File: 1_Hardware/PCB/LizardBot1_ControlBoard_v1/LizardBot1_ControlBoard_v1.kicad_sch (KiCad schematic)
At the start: 0 parts

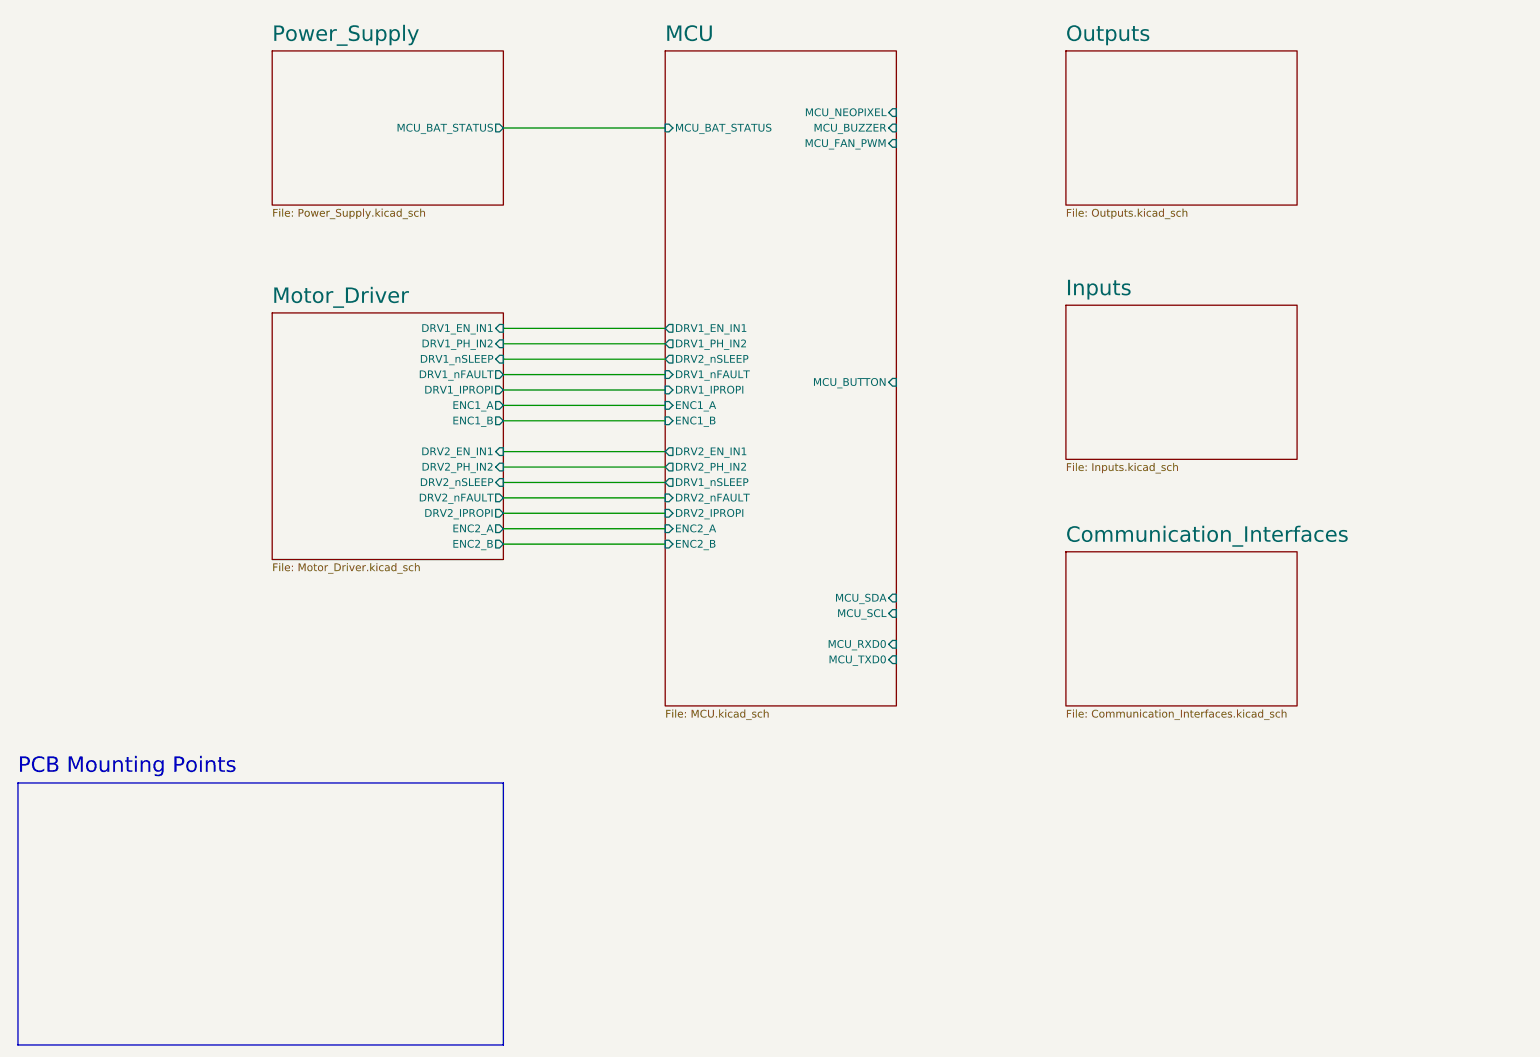
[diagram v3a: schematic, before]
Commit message: Added Peripherals schematic
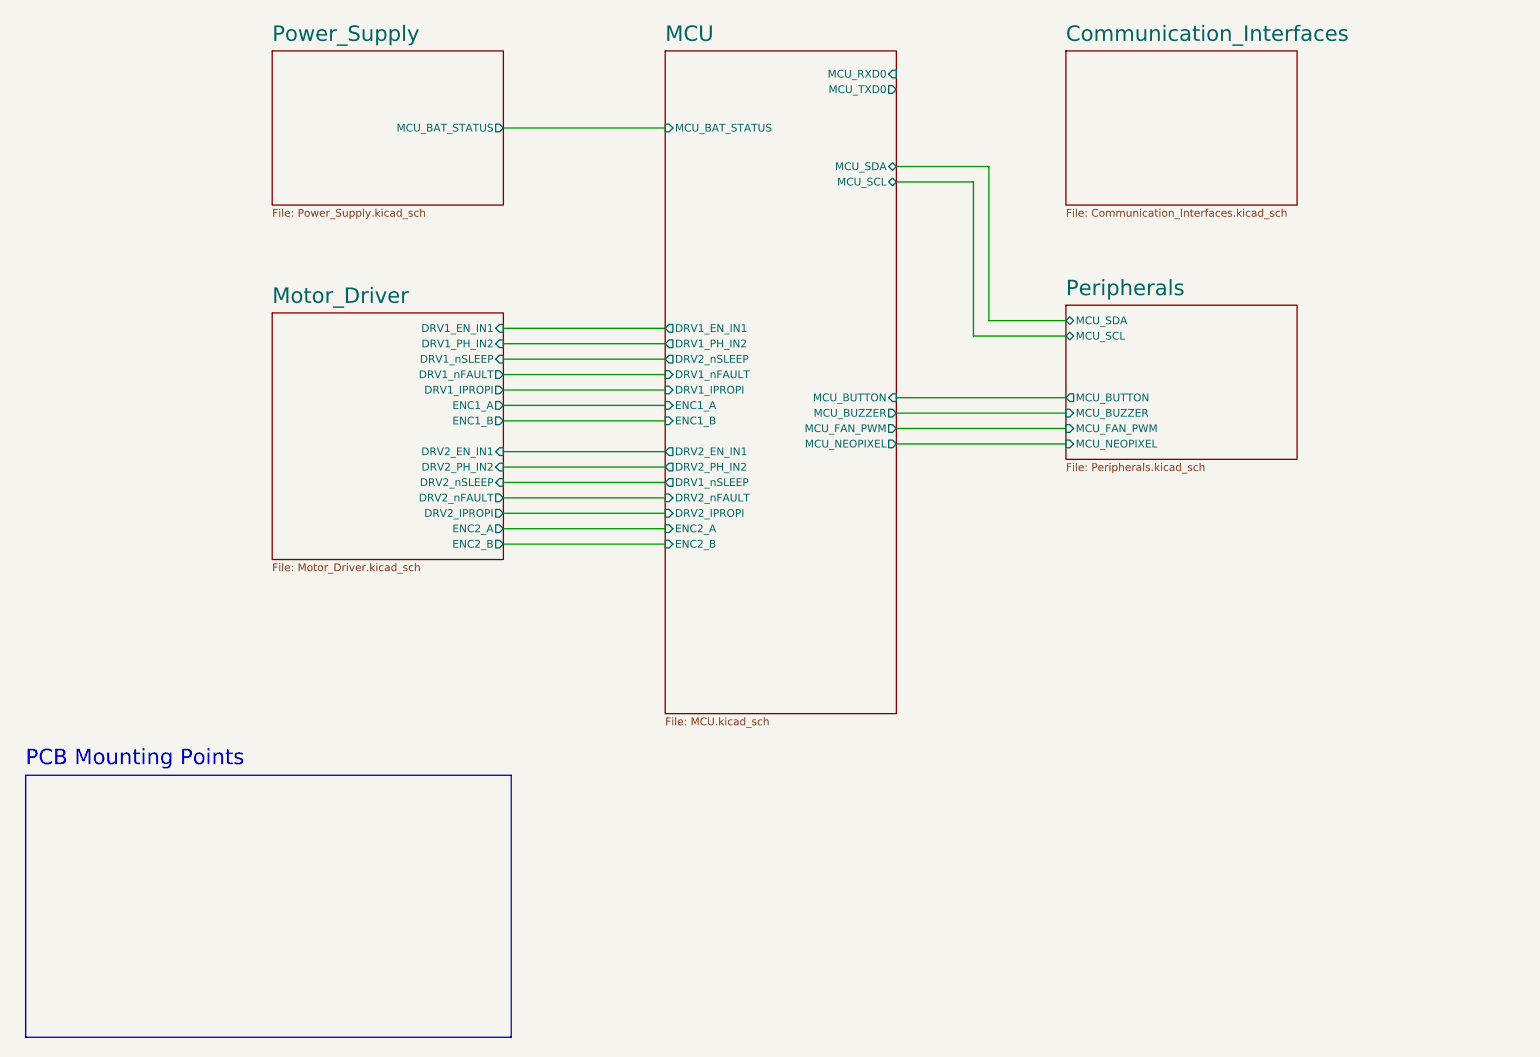
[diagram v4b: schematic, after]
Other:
- sheet Outputs renamed Peripherals
- removed sheet Inputs
- sheet Peripherals: file Outputs.kicad_sch -> Peripherals.kicad_sch
- sheet Peripherals ports: added MCU_BUTTON, MCU_BUZZER, MCU_FAN_PWM, MCU_NEOPIXEL, MCU_SCL, MCU_SDA; removed none
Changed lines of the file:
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@@
+	(wire
+		(pts
+			(xy 163.83 87.63) (xy 191.77 87.63)
+		)
+		(stroke
+			(width 0)
+			(type default)
+		)
+	)
 	(wire
 		(pts
@@
 	(wire
 		(pts
+			(xy 179.07 46.99) (xy 163.83 46.99)
+		)
+		(stroke
+			(width 0)
+			(type default)
+		)
+	)
+	(wire
+		(pts
 			(xy 99.06 93.98) (xy 125.73 93.98)
 		)
@@
 	(wire
 		(pts
+			(xy 163.83 85.09) (xy 191.77 85.09)
+		)
+		(stroke
+			(width 0)
+			(type default)
+		)
+	)
+	(wire
+		(pts
 			(xy 99.06 81.28) (xy 125.73 81.28)
 		)
@@
 	(wire
 		(pts
+			(xy 163.83 92.71) (xy 191.77 92.71)
+		)
+		(stroke
+			(width 0)
+			(type default)
+		)
+	)
+	(wire
+		(pts
 			(xy 99.06 40.64) (xy 125.73 40.64)
 		)
@@
 	(wire
 		(pts
+			(xy 176.53 74.93) (xy 191.77 74.93)
+		)
+		(stroke
+			(width 0)
+			(type default)
+		)
+	)
+	(wire
+		(pts
+			(xy 176.53 74.93) (xy 176.53 49.53)
+		)
+		(stroke
+			(width 0)
+			(type default)
+		)
+	)
+	(wire
+		(pts
+			(xy 163.83 90.17) (xy 191.77 90.17)
+		)
+		(stroke
+			(width 0)
+			(type default)
+		)
+	)
+	(wire
+		(pts
+			(xy 179.07 72.39) (xy 179.07 46.99)
+		)
+		(stroke
+			(width 0)
+			(type default)
+		)
+	)
+	(wire
+		(pts
+			(xy 179.07 72.39) (xy 191.77 72.39)
+		)
+		(stroke
+			(width 0)
+			(type default)
+		)
+	)
+	(wire
+		(pts
+			(xy 176.53 49.53) (xy 163.83 49.53)
+		)
+		(stroke
+			(width 0)
+			(type default)
+		)
+	)
+	(wire
+		(pts
 			(xy 99.06 106.68) (xy 125.73 106.68)
 		)
@@
 	)
 	(rectangle
-		(start 19.05 148.59)
-		(end 99.06 191.77)
+		(start 20.32 147.32)
+		(end 100.33 190.5)
 		(stroke
 			(width 0)
@@
 	(text "PCB Mounting Points"
 		(exclude_from_sim no)
-		(at 19.05 147.32 0)
+		(at 20.32 146.05 0)
 		(effects
 			(font
@@
 	)
 	(sheet
-		(at 191.77 69.85)
-		(size 38.1 25.4)
+		(at 125.73 27.94)
+		(size 38.1 109.22)
 		(fields_autoplaced yes)
 		(stroke
@@
 			(color 0 0 0 0.0000)
 		)
-		(property "Sheetname" "Inputs"
-			(at 191.77 68.5034 0)
-			(effects
-				(font
-					(size 2.54 2.54)
-				)
-				(justify left bottom)
-			)
-		)
-		(property "Sheetfile" "Inputs.kicad_sch"
-			(at 191.77 95.8346 0)
-			(effects
-				(font
-					(size 1.27 1.27)
-				)
-				(justify left top)
-			)
-		)
-		(instances
-			(project "LizardBot1_ControlBoard_v1"
-				(path "/1a674a4d-d877-4d7a-ad57-e0a054705c31"
-					(page "5")
-				)
-			)
-		)
-	)
-	(sheet
-		(at 125.73 27.94)
-		(size 38.1 107.95)
-		(fields_autoplaced yes)
-		(stroke
-			(width 0.1524)
-			(type solid)
-		)
-		(fill
-			(color 0 0 0 0.0000)
-		)
 		(property "Sheetname" "MCU"
 			(at 125.73 26.5934 0)
@@
 		)
 		(property "Sheetfile" "MCU.kicad_sch"
-			(at 125.73 136.4746 0)
+			(at 125.73 137.7446 0)
 			(effects
 				(font
@@
 			)
 		)
+		(pin "MCU_BUZZER" output
+			(at 163.83 87.63 0)
+			(effects
+				(font
+					(size 1.27 1.27)
+				)
+				(justify right)
+			)
+		)
+		(pin "MCU_FAN_PWM" output
+			(at 163.83 90.17 0)
+			(effects
+				(font
+					(size 1.27 1.27)
+				)
+				(justify right)
+			)
+		)
+		(pin "MCU_NEOPIXEL" output
+			(at 163.83 92.71 0)
+			(effects
+				(font
+					(size 1.27 1.27)
+				)
+				(justify right)
+			)
+		)
+		(pin "MCU_BUTTON" input
+			(at 163.83 85.09 0)
+			(effects
+				(font
+					(size 1.27 1.27)
+				)
+				(justify right)
+			)
+		)
+		(pin "MCU_SDA" bidirectional
+			(at 163.83 46.99 0)
+			(effects
+				(font
+					(size 1.27 1.27)
+				)
+				(justify right)
+			)
+		)
+		(pin "MCU_SCL" bidirectional
+			(at 163.83 49.53 0)
+			(effects
+				(font
+					(size 1.27 1.27)
+				)
+				(justify right)
+			)
+		)
 		(pin "MCU_RXD0" input
-			(at 163.83 125.73 0)
-			(effects
-				(font
-					(size 1.27 1.27)
-				)
-				(justify right)
-			)
-		)
-		(pin "MCU_TXD0" input
-			(at 163.83 128.27 0)
-			(effects
-				(font
-					(size 1.27 1.27)
-				)
-				(justify right)
-			)
-		)
-		(pin "MCU_NEOPIXEL" input
-			(at 163.83 38.1 0)
-			(effects
-				(font
-					(size 1.27 1.27)
-				)
-				(justify right)
-			)
-		)
-		(pin "MCU_BUZZER" input
-			(at 163.83 40.64 0)
-			(effects
-				(font
-					(size 1.27 1.27)
-				)
-				(justify right)
-			)
-		)
-		(pin "MCU_BUTTON" input
-			(at 163.83 82.55 0)
-			(effects
-				(font
-					(size 1.27 1.27)
-				)
-				(justify right)
-			)
-		)
-		(pin "MCU_SCL" input
-			(at 163.83 120.65 0)
-			(effects
-				(font
-					(size 1.27 1.27)
-				)
-				(justify right)
-			)
-		)
-		(pin "MCU_SDA" input
-			(at 163.83 118.11 0)
-			(effects
-				(font
-					(size 1.27 1.27)
-				)
-				(justify right)
-			)
-		)
-		(pin "MCU_FAN_PWM" input
-			(at 163.83 43.18 0)
+			(at 163.83 31.75 0)
+			(effects
+				(font
+					(size 1.27 1.27)
+				)
+				(justify right)
+			)
+		)
+		(pin "MCU_TXD0" output
+			(at 163.83 34.29 0)
 			(effects
 				(font
@@
 	)
 	(sheet
-		(at 191.77 27.94)
+		(at 191.77 69.85)
 		(size 38.1 25.4)
 		(fields_autoplaced yes)
@@
 			(color 0 0 0 0.0000)
 		)
-		(property "Sheetname" "Outputs"
-			(at 191.77 26.5934 0)
+		(property "Sheetname" "Peripherals"
+			(at 191.77 68.5034 0)
 			(effects
 				(font
@@
 			)
 		)
-		(property "Sheetfile" "Outputs.kicad_sch"
-			(at 191.77 53.9246 0)
+		(property "Sheetfile" "Peripherals.kicad_sch"
+			(at 191.77 95.8346 0)
 			(effects
 				(font
@@
 				)
 				(justify left top)
+			)
+		)
+		(pin "MCU_BUZZER" input
+			(at 191.77 87.63 180)
+			(effects
+				(font
+					(size 1.27 1.27)
+				)
+				(justify left)
+			)
+		)
+		(pin "MCU_FAN_PWM" input
+			(at 191.77 90.17 180)
+			(effects
+				(font
+					(size 1.27 1.27)
+				)
+				(justify left)
+			)
+		)
+		(pin "MCU_NEOPIXEL" input
+			(at 191.77 92.71 180)
+			(effects
+				(font
+					(size 1.27 1.27)
+				)
+				(justify left)
+			)
+		)
+		(pin "MCU_SCL" bidirectional
+			(at 191.77 74.93 180)
+			(effects
+				(font
+					(size 1.27 1.27)
+				)
+				(justify left)
+			)
+		)
+		(pin "MCU_SDA" bidirectional
+			(at 191.77 72.39 180)
+			(effects
+				(font
+					(size 1.27 1.27)
+				)
+				(justify left)
+			)
+		)
+		(pin "MCU_BUTTON" output
+			(at 191.77 85.09 180)
+			(effects
+				(font
+					(size 1.27 1.27)
+				)
+				(justify left)
 			)
 		)
@@
 	)
 	(sheet
-		(at 191.77 110.49)
+		(at 191.77 27.94)
 		(size 38.1 25.4)
 		(fields_autoplaced yes)
@@
 		)
 		(property "Sheetname" "Communication_Interfaces"
-			(at 191.77 109.1434 0)
+			(at 191.77 26.5934 0)
 			(effects
 				(font
@@
 		)
 		(property "Sheetfile" "Communication_Interfaces.kicad_sch"
-			(at 191.77 136.4746 0)
-			(effects
-				(font
+			(at 191.77 53.9246 0)
+			(effects
+				(font

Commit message: Added Communication_Interfaces schematic
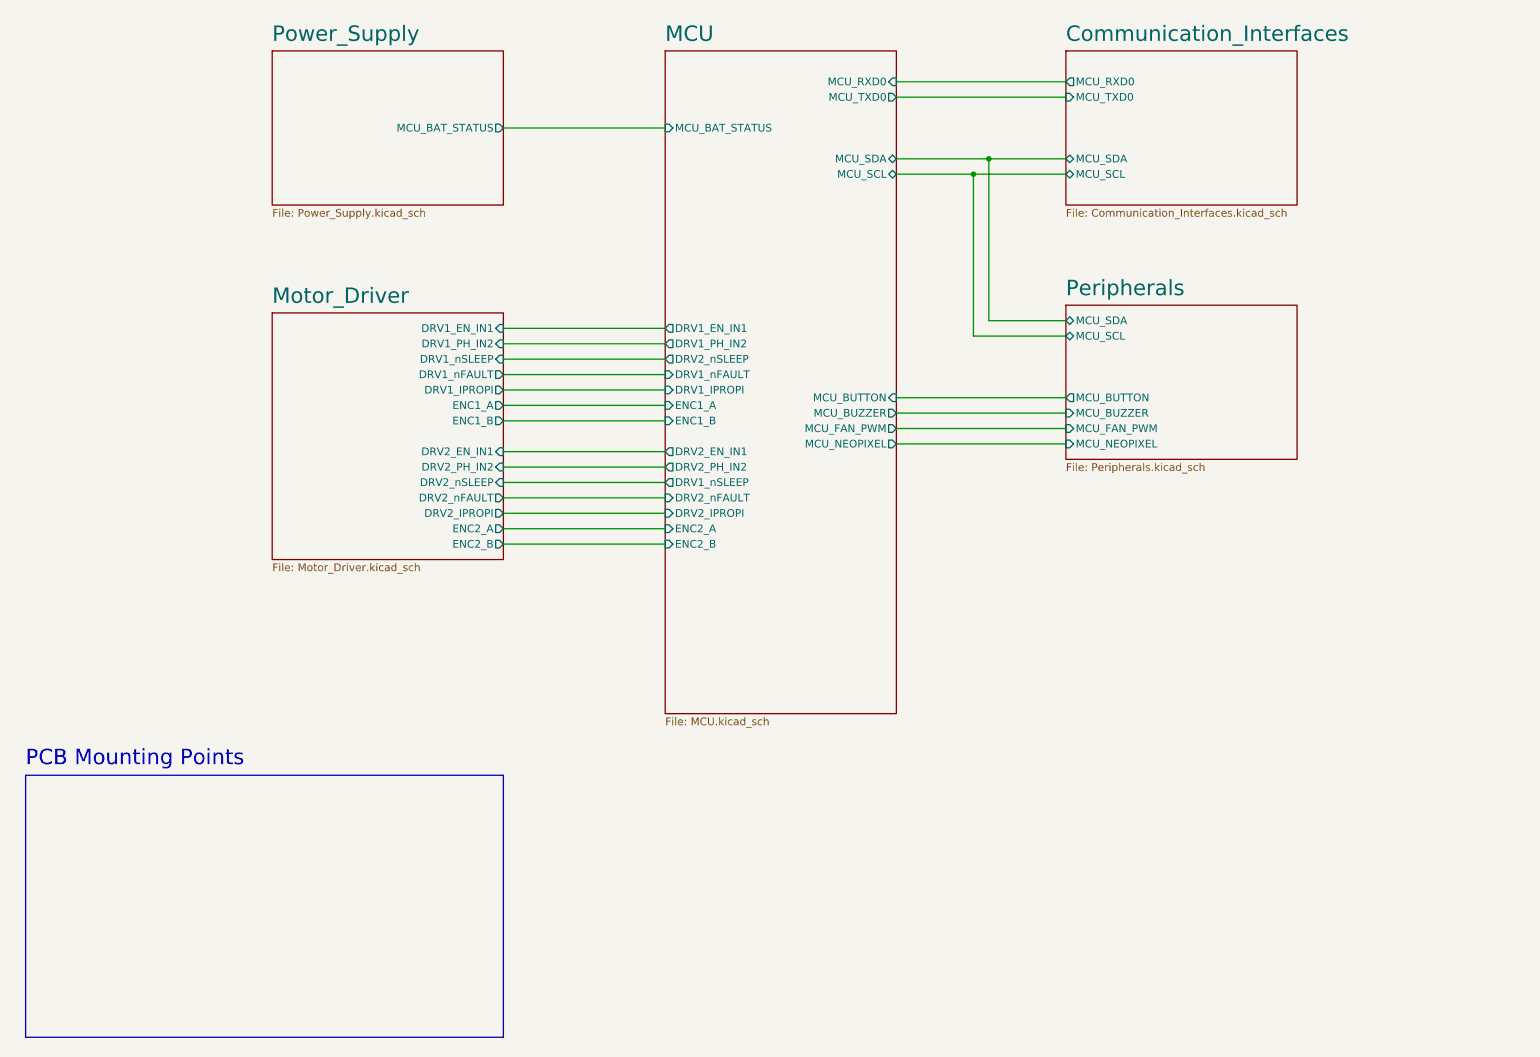
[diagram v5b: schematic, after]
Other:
- sheet Communication_Interfaces ports: added MCU_RXD0, MCU_SCL, MCU_SDA, MCU_TXD0; removed none
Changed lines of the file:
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@@
 		(comment 1 "Designed by: Manuel Lagarto")
 	)
+	(junction
+		(at 176.53 48.26)
+		(diameter 0)
+		(color 0 0 0 0)
+	)
+	(junction
+		(at 179.07 45.72)
+		(diameter 0)
+		(color 0 0 0 0)
+	)
 	(wire
 		(pts
@@
 	(wire
 		(pts
-			(xy 179.07 46.99) (xy 163.83 46.99)
+			(xy 179.07 45.72) (xy 163.83 45.72)
 		)
 		(stroke
@@
 	(wire
 		(pts
+			(xy 163.83 33.02) (xy 191.77 33.02)
+		)
+		(stroke
+			(width 0)
+			(type default)
+		)
+	)
+	(wire
+		(pts
 			(xy 99.06 81.28) (xy 125.73 81.28)
 		)
@@
 	(wire
 		(pts
+			(xy 176.53 48.26) (xy 191.77 48.26)
+		)
+		(stroke
+			(width 0)
+			(type default)
+		)
+	)
+	(wire
+		(pts
 			(xy 99.06 109.22) (xy 125.73 109.22)
 		)
@@
 	(wire
 		(pts
-			(xy 176.53 74.93) (xy 176.53 49.53)
+			(xy 176.53 74.93) (xy 176.53 48.26)
 		)
 		(stroke
@@
 	(wire
 		(pts
-			(xy 179.07 72.39) (xy 179.07 46.99)
+			(xy 179.07 72.39) (xy 179.07 45.72)
 		)
 		(stroke
@@
 	(wire
 		(pts
-			(xy 176.53 49.53) (xy 163.83 49.53)
+			(xy 163.83 35.56) (xy 191.77 35.56)
+		)
+		(stroke
+			(width 0)
+			(type default)
+		)
+	)
+	(wire
+		(pts
+			(xy 176.53 48.26) (xy 163.83 48.26)
 		)
 		(stroke
@@
 		(pts
 			(xy 99.06 99.06) (xy 125.73 99.06)
+		)
+		(stroke
+			(width 0)
+			(type default)
+		)
+	)
+	(wire
+		(pts
+			(xy 179.07 45.72) (xy 191.77 45.72)
 		)
 		(stroke
@@
 	(rectangle
 		(start 20.32 147.32)
-		(end 100.33 190.5)
+		(end 99.06 190.5)
 		(stroke
 			(width 0)
@@
 		)
 		(pin "MCU_SDA" bidirectional
-			(at 163.83 46.99 0)
+			(at 163.83 45.72 0)
 			(effects
 				(font
@@
 		)
 		(pin "MCU_SCL" bidirectional
-			(at 163.83 49.53 0)
+			(at 163.83 48.26 0)
 			(effects
 				(font
@@
 		)
 		(pin "MCU_RXD0" input
-			(at 163.83 31.75 0)
+			(at 163.83 33.02 0)
 			(effects
 				(font
@@
 		)
 		(pin "MCU_TXD0" output
-			(at 163.83 34.29 0)
+			(at 163.83 35.56 0)
 			(effects
 				(font
@@
 			(project "LizardBot1_ControlBoard_v1"
 				(path "/1a674a4d-d877-4d7a-ad57-e0a054705c31"
-					(page "6")
+					(page "5")
 				)
 			)
@@
 			)
 		)
+		(pin "MCU_SDA" bidirectional
+			(at 191.77 45.72 180)
+			(effects
+				(font
+					(size 1.27 1.27)
+				)
+				(justify left)
+			)
+		)
+		(pin "MCU_SCL" bidirectional
+			(at 191.77 48.26 180)
+			(effects
+				(font
+					(size 1.27 1.27)
+				)
+				(justify left)
+			)
+		)
+		(pin "MCU_RXD0" output
+			(at 191.77 33.02 180)
+			(effects
+				(font
+					(size 1.27 1.27)
+				)
+				(justify left)
+			)
+		)
+		(pin "MCU_TXD0" input
+			(at 191.77 35.56 180)
+			(effects
+				(font
+					(size 1.27 1.27)
+				)
+				(justify left)
+			)
+		)
 		(instances
 			(project "LizardBot1_ControlBoard_v1"
 				(path "/1a674a4d-d877-4d7a-ad57-e0a054705c31"
-					(page "7")
-				)
-			)
+					(page "6")
+				)
+			)

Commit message: PCB schematics revision
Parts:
- added TP101: BATT_TP, symbol Connector:TestPoint
- added TP102: 12V_TP, symbol Connector:TestPoint
- added TP103: 5V_TP, symbol Connector:TestPoint
- added TP104: 3V3_TP, symbol Connector:TestPoint
- added TP105: 1V8_TP, symbol Connector:TestPoint
- added TP106: GND_TP, symbol Connector:TestPoint
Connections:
- new net +12V: TP102.1
- new net +1V8: TP105.1
- new net +3V3: TP104.1
- new net +5V: TP103.1
- new net +BATT: TP101.1
- new net GND: TP106.1
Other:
- note added: "(!) TODO (!) DONE 1. Hierarchical labels separated from labels DONE 2. Power flags & test points in root page DONE 3. Choose polyfuse and fuse components 4. Review LED colors and resistors 5. Label undefined nets"
